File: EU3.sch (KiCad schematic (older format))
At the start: 52 parts, among them J301 ClockOut, J303 ClockIn, J304 Out0, J305 Out1, J306 Out2, J307 Out3, J308 Out4, J309 Out5, J310 Out6, J311 Out7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

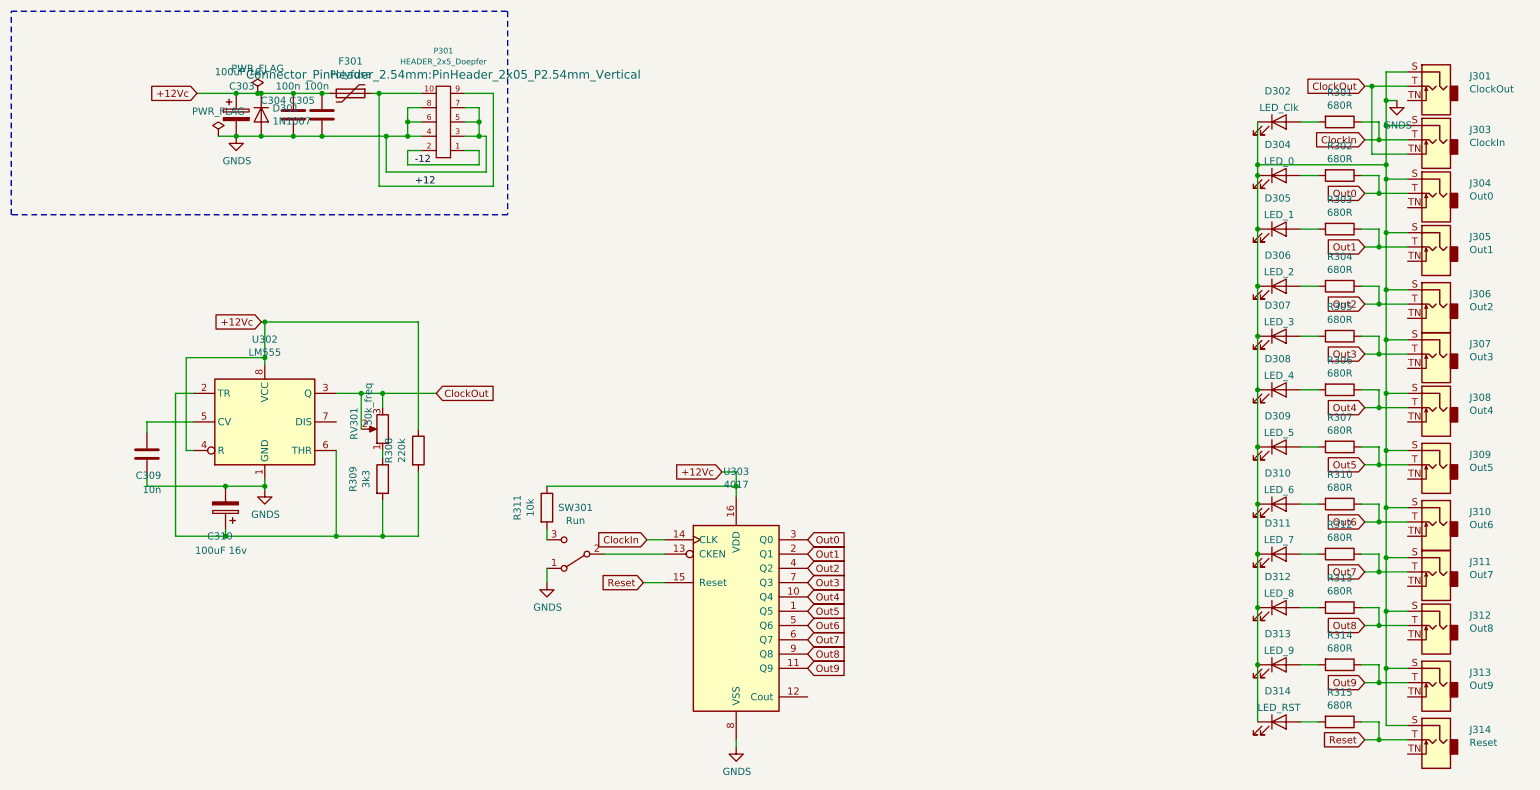
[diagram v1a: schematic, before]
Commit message: Counter with input protection and new stop/carry feature
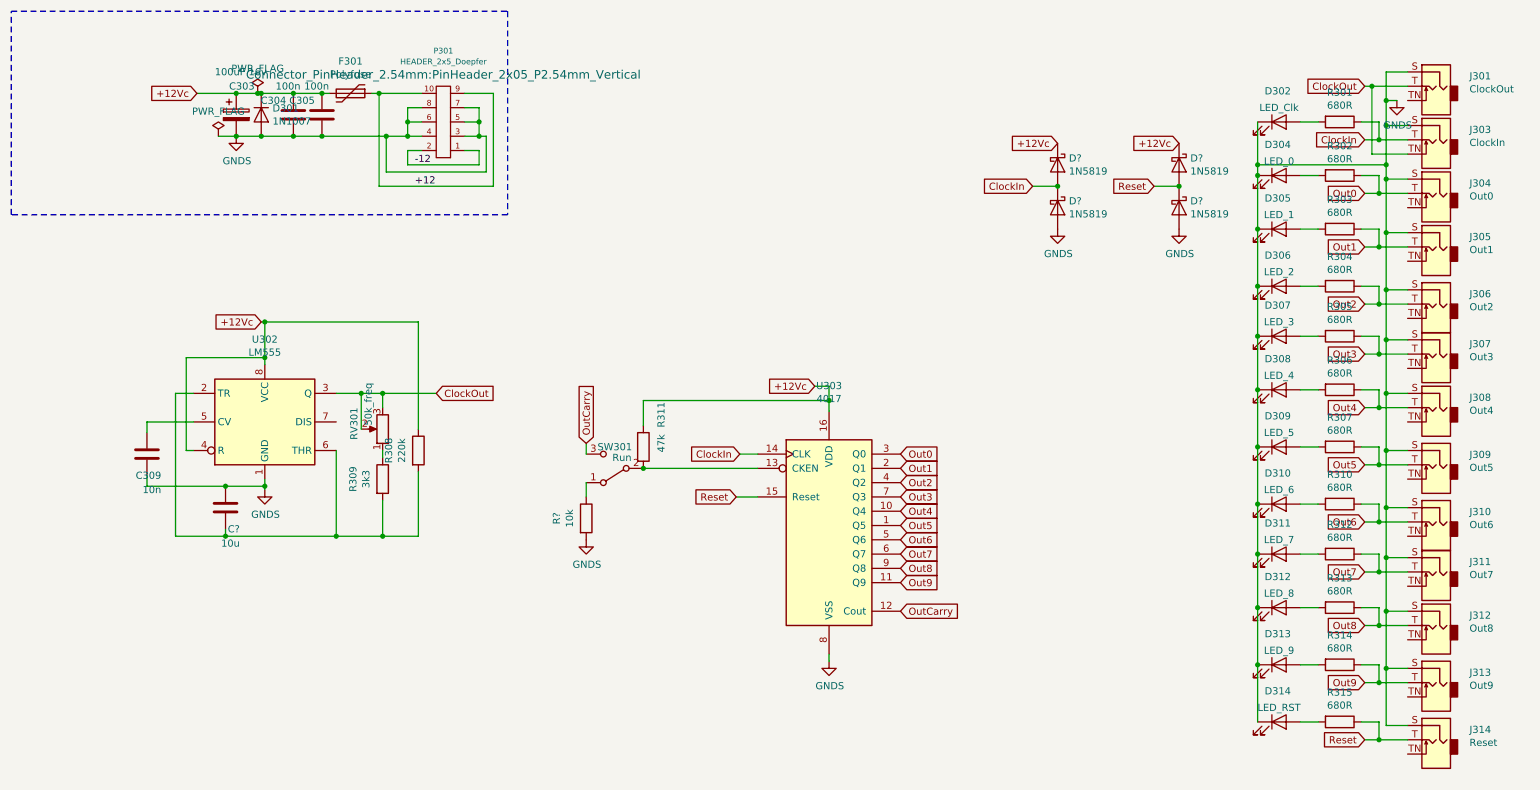
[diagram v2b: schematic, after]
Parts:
- removed C310: 100uF 16v, Capacitor_THT:CP_Radial_D5.0mm_P2.50mm, symbol Device:CP
- added C?: 10u, Capacitor_SMD:C_0805_2012Metric_Pad1.15x1.40mm_HandSolder, symbol Device:C
- added D? (x4): 1N5819, Diode_THT:D_DO-41_SOD81_P10.16mm_Horizontal, symbol Diode:1N5819
- added R?: 10k, Resistor_SMD:R_0805_2012Metric_Pad1.15x1.40mm_HandSolder, symbol Device:R
- R311: value 10k -> 47k
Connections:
- net +12Vc: now also D?.1 (K), D?.1 (K)
- net ClockIn: now also D?.1 (K), D?.2 (A)
- net GNDS: now also C?.2, D?.2 (A), D?.2 (A), R?.2; no longer SW301.1 (A)
- net Reset: now also D?.1 (K), D?.2 (A)
- net at R308.2, R309.2, U302.2 (TR)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: now also C?.1
- net OutCarry: now reaches U303.12 (Cout)
- net OutCarry: now also SW301.3 (C)
- net at SW301.2 (B), U303.13 (CKEN): now also R311.2
- new net: R?.1, SW301.1 (A)
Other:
- moved on the sheet: R311, SW301, U303
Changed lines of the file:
@@
 L 4xxx:4017 U303
 U 1 1 5C7AF44B
-P 5650 4725
-F 0 "U303" H 5650 5703 50  0000 C CNN
-F 1 "4017" H 5650 5612 50  0000 C CNN
-F 2 "Package_SO:SOIC-16_4.55x10.3mm_P1.27mm" H 5650 4725 50  0001 C CNN
-F 3 "http://www.intersil.com/content/dam/Intersil/documents/cd40/cd4017bms-22bms.pdf" H 5650 4725 50  0001 C CNN
-	1    5650 4725
+P 6300 4125
+F 0 "U303" H 6300 5103 50  0000 C CNN
+F 1 "4017" H 6300 5012 50  0000 C CNN
+F 2 "Package_SO:SOIC-16_4.55x10.3mm_P1.27mm" H 6300 4125 50  0001 C CNN
+F 3 "http://www.intersil.com/content/dam/Intersil/documents/cd40/cd4017bms-22bms.pdf" H 6300 4125 50  0001 C CNN
+	1    6300 4125
 	1    0    0    -1
 $EndComp
@@
 Wire Wire Line
 	1525 3775 1525 3850
-Wire Wire Line
-	1525 3850 2075 3850
 Connection ~ 2350 3850
 Wire Wire Line
 	2350 3850 2350 3800
-$Comp
-L Device:CP C?
-U 1 1 5C7BA0E3
-P 2075 4000
-AR Path="/5C7BA0E3" Ref="C?"  Part="1"
-AR Path="/5C781441/5C7BA0E3" Ref="C310"  Part="1"
-F 0 "C310" H 2025 4200 50  0000 L CNN
-F 1 "100uF 16v" H 1925 4300 50  0000 L CNN
-F 2 "Capacitor_THT:CP_Radial_D5.0mm_P2.50mm" H 2113 3850 50  0001 C CNN
-F 3 "~" H 2075 4000 50  0001 C CNN
-	1    2075 4000
-	-1   0    0    1
-$EndComp
-Connection ~ 2075 3850
-Wire Wire Line
-	2075 3850 2350 3850
 Wire Wire Line
 	2075 4200 2075 4150
@@
 Wire Wire Line
 	10050 1425 10150 1425
-Text GLabel 5025 4225 0    50   Input ~ 0
+Text GLabel 5675 3625 0    50   Input ~ 0
 ClockIn
 $Comp
@@
 Connection ~ 9300 3575
 Connection ~ 10200 3600
-Text GLabel 6150 5125 2    50   Input ~ 0
+Text GLabel 6800 4525 2    50   Input ~ 0
 Out9
-Text GLabel 6150 5025 2    50   Input ~ 0
+Text GLabel 6800 4425 2    50   Input ~ 0
 Out8
-Text GLabel 6150 4925 2    50   Input ~ 0
+Text GLabel 6800 4325 2    50   Input ~ 0
 Out7
-Text GLabel 6150 4825 2    50   Input ~ 0
+Text GLabel 6800 4225 2    50   Input ~ 0
 Out6
-Text GLabel 6150 4625 2    50   Input ~ 0
+Text GLabel 6800 4025 2    50   Input ~ 0
 Out4
-Text GLabel 6150 4525 2    50   Input ~ 0
+Text GLabel 6800 3925 2    50   Input ~ 0
 Out3
-Text GLabel 6150 4425 2    50   Input ~ 0
+Text GLabel 6800 3825 2    50   Input ~ 0
 Out2
-Text GLabel 6150 4325 2    50   Input ~ 0
+Text GLabel 6800 3725 2    50   Input ~ 0
 Out1
-Text GLabel 6150 4725 2    50   Input ~ 0
+Text GLabel 6800 4125 2    50   Input ~ 0
 Out5
-Text GLabel 6150 4225 2    50   Input ~ 0
+Text GLabel 6800 3625 2    50   Input ~ 0
 Out0
 $Comp
@@
 Connection ~ 9300 5100
 Connection ~ 10200 5125
-Text GLabel 5000 4525 0    50   Input ~ 0
+Text GLabel 5650 3925 0    50   Input ~ 0
 Reset
 Wire Wire Line
-	5025 4225 5150 4225
-Wire Wire Line
-	5000 4525 5150 4525
-Text GLabel 5550 3750 0    50   Input ~ 0
+	5675 3625 5800 3625
+Wire Wire Line
+	5650 3925 5800 3925
+Text GLabel 6200 3150 0    50   Input ~ 0
 +12Vc
 $Comp
 L power:GNDS #PWR?
 U 1 1 5C879D20
-P 5650 5675
+P 6300 5075
 AR Path="/5C879D20" Ref="#PWR?"  Part="1"
 AR Path="/5D60ED9A/5C879D20" Ref="#PWR?"  Part="1"
 AR Path="/5C781441/5C879D20" Ref="#PWR0124"  Part="1"
-F 0 "#PWR0124" H 5650 5425 50  0001 C CNN
-F 1 "GNDS" H 5655 5502 50  0000 C CNN
-F 2 "" H 5650 5675 50  0001 C CNN
-F 3 "" H 5650 5675 50  0001 C CNN
-	1    5650 5675
-	1    0    0    -1
-$EndComp
-Wire Wire Line
-	5650 5675 5650 5625
-Wire Wire Line
-	5650 3925 5650 3850
-Wire Wire Line
-	5650 3750 5550 3750
+F 0 "#PWR0124" H 6300 4825 50  0001 C CNN
+F 1 "GNDS" H 6305 4902 50  0000 C CNN
+F 2 "" H 6300 5075 50  0001 C CNN
+F 3 "" H 6300 5075 50  0001 C CNN
+	1    6300 5075
+	1    0    0    -1
+$EndComp
+Wire Wire Line
+	6300 5075 6300 5025
+Wire Wire Line
+	6300 3325 6300 3250
+Wire Wire Line
+	6300 3150 6200 3150
 $Comp
 L Switch:SW_SPDT SW?
 U 1 1 5C88D8DA
-P 4525 4325
+P 4800 3725
 AR Path="/5C88D8DA" Ref="SW?"  Part="1"
 AR Path="/5C781441/5C88D8DA" Ref="SW301"  Part="1"
-F 0 "SW301" H 4525 4000 50  0000 C CNN
-F 1 "Run" H 4525 4091 50  0000 C CNN
-F 2 "AJ-Dropbox-Kicad:SP1MS1" H 4525 4325 50  0001 C CNN
-F 3 "~" H 4525 4325 50  0001 C CNN
-	1    4525 4325
+F 0 "SW301" H 4800 3575 50  0000 C CNN
+F 1 "Run" H 4750 3650 50  0000 C CNN
+F 2 "AJ-Dropbox-Kicad:SP1MS1" H 4800 3725 50  0001 C CNN
+F 3 "~" H 4800 3725 50  0001 C CNN
+	1    4800 3725
 	-1   0    0    1
 $EndComp
-Wire Wire Line
-	5150 4325 4725 4325
 $Comp
 L Device:R R?
 U 1 1 5C8AA357
-P 4325 4000
+P 5000 3575
 AR Path="/5C8AA357" Ref="R?"  Part="1"
 AR Path="/5C781441/5C8AA357" Ref="R311"  Part="1"
-F 0 "R311" V 4118 4000 50  0000 C CNN
-F 1 "10k" V 4209 4000 50  0000 C CNN
-F 2 "Resistor_SMD:R_0805_2012Metric_Pad1.15x1.40mm_HandSolder" V 4255 4000 50  0001 C CNN
-F 3 "~" H 4325 4000 50  0001 C CNN
-	1    4325 4000
+F 0 "R311" V 5125 3800 50  0000 C CNN
+F 1 "47k" V 5125 3600 50  0000 C CNN
+F 2 "Resistor_SMD:R_0805_2012Metric_Pad1.15x1.40mm_HandSolder" V 4930 3575 50  0001 C CNN
+F 3 "~" H 5000 3575 50  0001 C CNN
+	1    5000 3575
 	1    0    0    -1
 $EndComp
@@
 L power:GNDS #PWR?
 U 1 1 5C8AA43A
-P 4325 4525
+P 4600 4225
 AR Path="/5C8AA43A" Ref="#PWR?"  Part="1"
 AR Path="/5D60ED9A/5C8AA43A" Ref="#PWR?"  Part="1"
 AR Path="/5C781441/5C8AA43A" Ref="#PWR0125"  Part="1"
-F 0 "#PWR0125" H 4325 4275 50  0001 C CNN
-F 1 "GNDS" H 4330 4352 50  0000 C CNN
-F 2 "" H 4325 4525 50  0001 C CNN
-F 3 "" H 4325 4525 50  0001 C CNN
-	1    4325 4525
-	1    0    0    -1
-$EndComp
-Wire Wire Line
-	4325 3850 5650 3850
-Connection ~ 5650 3850
-Wire Wire Line
-	5650 3850 5650 3750
-Wire Wire Line
-	4325 4150 4325 4225
-Wire Wire Line
-	4325 4525 4325 4425
+F 0 "#PWR0125" H 4600 3975 50  0001 C CNN
+F 1 "GNDS" H 4605 4052 50  0000 C CNN
+F 2 "" H 4600 4225 50  0001 C CNN
+F 3 "" H 4600 4225 50  0001 C CNN
+	1    4600 4225
+	1    0    0    -1
+$EndComp
+Connection ~ 6300 3250
+Wire Wire Line
+	6300 3250 6300 3150
+Wire Wire Line
+	4600 3550 4600 3625
+Wire Wire Line
+	4600 3925 4600 3825
 Wire Wire Line
 	1875 1100 2150 1100
@@
 Text Label 3400 1750 0    50   ~ 0
 +12
+Text GLabel 7725 1750 0    50   Input ~ 0
+ClockIn
+Text GLabel 8575 1750 0    50   Input ~ 0
+Reset
+$Comp
+L Diode:1N5819 D?
+U 1 1 5CCD6095
+P 7900 1600
+F 0 "D?" V 7854 1679 50  0000 L CNN
+F 1 "1N5819" V 7945 1679 50  0000 L CNN
+F 2 "Diode_THT:D_DO-41_SOD81_P10.16mm_Horizontal" H 7900 1425 50  0001 C CNN
+F 3 "http://www.vishay.com/docs/88525/1n5817.pdf" H 7900 1600 50  0001 C CNN
+	1    7900 1600
+	0    1    1    0
+$EndComp
+$Comp
+L Diode:1N5819 D?
+U 1 1 5CCD6FDF
+P 7900 1900
+F 0 "D?" V 7854 1979 50  0000 L CNN
+F 1 "1N5819" V 7945 1979 50  0000 L CNN
+F 2 "Diode_THT:D_DO-41_SOD81_P10.16mm_Horizontal" H 7900 1725 50  0001 C CNN
+F 3 "http://www.vishay.com/docs/88525/1n5817.pdf" H 7900 1900 50  0001 C CNN
+	1    7900 1900
+	0    1    1    0
+$EndComp
+$Comp
+L power:GNDS #PWR?
+U 1 1 5CCD768A
+P 7900 2050
+AR Path="/5CCD768A" Ref="#PWR?"  Part="1"
+AR Path="/5D60ED9A/5CCD768A" Ref="#PWR?"  Part="1"
+AR Path="/5C781441/5CCD768A" Ref="#PWR?"  Part="1"
+F 0 "#PWR?" H 7900 1800 50  0001 C CNN
+F 1 "GNDS" H 7905 1877 50  0000 C CNN
+F 2 "" H 7900 2050 50  0001 C CNN
+F 3 "" H 7900 2050 50  0001 C CNN
+	1    7900 2050
+	1    0    0    -1
+$EndComp
+Text GLabel 7900 1450 0    50   Input ~ 0
++12Vc
+Wire Wire Line
+	7725 1750 7900 1750
+Connection ~ 7900 1750
+$Comp
+L Diode:1N5819 D?
+U 1 1 5CCE2123
+P 8750 1600
+F 0 "D?" V 8704 1679 50  0000 L CNN
+F 1 "1N5819" V 8795 1679 50  0000 L CNN
+F 2 "Diode_THT:D_DO-41_SOD81_P10.16mm_Horizontal" H 8750 1425 50  0001 C CNN
+F 3 "http://www.vishay.com/docs/88525/1n5817.pdf" H 8750 1600 50  0001 C CNN
+	1    8750 1600
+	0    1    1    0
+$EndComp
+$Comp
+L Diode:1N5819 D?
+U 1 1 5CCE212D
+P 8750 1900
+F 0 "D?" V 8704 1979 50  0000 L CNN
+F 1 "1N5819" V 8795 1979 50  0000 L CNN
+F 2 "Diode_THT:D_DO-41_SOD81_P10.16mm_Horizontal" H 8750 1725 50  0001 C CNN
+F 3 "http://www.vishay.com/docs/88525/1n5817.pdf" H 8750 1900 50  0001 C CNN
+	1    8750 1900
+	0    1    1    0
+$EndComp
+$Comp
+L power:GNDS #PWR?
+U 1 1 5CCE2137
+P 8750 2050
+AR Path="/5CCE2137" Ref="#PWR?"  Part="1"
+AR Path="/5D60ED9A/5CCE2137" Ref="#PWR?"  Part="1"
+AR Path="/5C781441/5CCE2137" Ref="#PWR?"  Part="1"
+F 0 "#PWR?" H 8750 1800 50  0001 C CNN
+F 1 "GNDS" H 8755 1877 50  0000 C CNN
+F 2 "" H 8750 2050 50  0001 C CNN
+F 3 "" H 8750 2050 50  0001 C CNN
+	1    8750 2050
+	1    0    0    -1
+$EndComp
+Text GLabel 8750 1450 0    50   Input ~ 0
++12Vc
+Wire Wire Line
+	8575 1750 8750 1750
+Connection ~ 8750 1750
+Wire Wire Line
+	5000 3725 5800 3725
+Wire Wire Line
+	5000 3425 5000 3250
+Wire Wire Line
+	5000 3250 6300 3250
+Connection ~ 5000 3725
+Text GLabel 6800 4725 2    50   Input ~ 0
+OutCarry
+Text GLabel 4600 3550 1    50   Input ~ 0
+OutCarry
+$Comp
+L Device:R R?
+U 1 1 5CD1A27B
+P 4600 4075
+AR Path="/5CD1A27B" Ref="R?"  Part="1"
+AR Path="/5C781441/5CD1A27B" Ref="R?"  Part="1"
+F 0 "R?" V 4393 4075 50  0000 C CNN
+F 1 "10k" V 4484 4075 50  0000 C CNN
+F 2 "Resistor_SMD:R_0805_2012Metric_Pad1.15x1.40mm_HandSolder" V 4530 4075 50  0001 C CNN
+F 3 "~" H 4600 4075 50  0001 C CNN
+	1    4600 4075
+	1    0    0    -1
+$EndComp
+Wire Wire Line
+	1525 3850 2075 3850
+$Comp
+L Device:C C?
+U 1 1 5CD1AA3C
+P 2075 4000
+AR Path="/5CD1AA3C" Ref="C?"  Part="1"
+AR Path="/5C781441/5CD1AA3C" Ref="C?"  Part="1"
+F 0 "C?" H 1975 4150 50  0000 L CNN
+F 1 "10u" H 1975 4250 50  0000 L CNN
+F 2 "Capacitor_SMD:C_0805_2012Metric_Pad1.15x1.40mm_HandSolder" H 2113 3850 50  0001 C CNN
+F 3 "~" H 2075 4000 50  0001 C CNN
+	1    2075 4000
+	-1   0    0    1
+$EndComp
+Connection ~ 2075 3850
+Wire Wire Line
+	2075 3850 2350 3850
 $EndSCHEMATC

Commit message: Rev 1,2 Counter Resistor on LED
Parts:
- R301, R302, R303, R304, R305, R306, R307, R310, R312, R313, R314, R315: value 680R -> 4k7
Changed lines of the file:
@@
 AR Path="/5C781441/5C7E5BC0" Ref="R301"  Part="1"
 F 0 "R301" V 9668 1300 50  0000 C CNN
-F 1 "680R" V 9759 1300 50  0000 C CNN
+F 1 "4k7" V 9759 1300 50  0000 C CNN
 F 2 "Resistor_SMD:R_0805_2012Metric_Pad1.15x1.40mm_HandSolder" V 9805 1300 50  0001 C CNN
 F 3 "~" H 9875 1300 50  0001 C CNN
@@
 AR Path="/5C781441/5C827C46" Ref="R302"  Part="1"
 F 0 "R302" V 9668 1675 50  0000 C CNN
-F 1 "680R" V 9759 1675 50  0000 C CNN
+F 1 "4k7" V 9759 1675 50  0000 C CNN
 F 2 "Resistor_SMD:R_0805_2012Metric_Pad1.15x1.40mm_HandSolder" V 9805 1675 50  0001 C CNN
 F 3 "~" H 9875 1675 50  0001 C CNN
@@
 AR Path="/5C781441/5C831A34" Ref="R303"  Part="1"
 F 0 "R303" V 9668 2050 50  0000 C CNN
-F 1 "680R" V 9759 2050 50  0000 C CNN
+F 1 "4k7" V 9759 2050 50  0000 C CNN
 F 2 "Resistor_SMD:R_0805_2012Metric_Pad1.15x1.40mm_HandSolder" V 9805 2050 50  0001 C CNN
 F 3 "~" H 9875 2050 50  0001 C CNN
@@
 AR Path="/5C781441/5C8355AA" Ref="R304"  Part="1"
 F 0 "R304" V 9668 2450 50  0000 C CNN
-F 1 "680R" V 9759 2450 50  0000 C CNN
+F 1 "4k7" V 9759 2450 50  0000 C CNN
 F 2 "Resistor_SMD:R_0805_2012Metric_Pad1.15x1.40mm_HandSolder" V 9805 2450 50  0001 C CNN
 F 3 "~" H 9875 2450 50  0001 C CNN
@@
 AR Path="/5C781441/5C83D871" Ref="R305"  Part="1"
 F 0 "R305" V 9668 2800 50  0000 C CNN
-F 1 "680R" V 9759 2800 50  0000 C CNN
+F 1 "4k7" V 9759 2800 50  0000 C CNN
 F 2 "Resistor_SMD:R_0805_2012Metric_Pad1.15x1.40mm_HandSolder" V 9805 2800 50  0001 C CNN
 F 3 "~" H 9875 2800 50  0001 C CNN
@@
 AR Path="/5C781441/5C83D884" Ref="R306"  Part="1"
 F 0 "R306" V 9668 3175 50  0000 C CNN
-F 1 "680R" V 9759 3175 50  0000 C CNN
+F 1 "4k7" V 9759 3175 50  0000 C CNN
 F 2 "Resistor_SMD:R_0805_2012Metric_Pad1.15x1.40mm_HandSolder" V 9805 3175 50  0001 C CNN
 F 3 "~" H 9875 3175 50  0001 C CNN
@@
 AR Path="/5C781441/5C83D897" Ref="R307"  Part="1"
 F 0 "R307" V 9668 3575 50  0000 C CNN
-F 1 "680R" V 9759 3575 50  0000 C CNN
+F 1 "4k7" V 9759 3575 50  0000 C CNN
 F 2 "Resistor_SMD:R_0805_2012Metric_Pad1.15x1.40mm_HandSolder" V 9805 3575 50  0001 C CNN
 F 3 "~" H 9875 3575 50  0001 C CNN
@@
 AR Path="/5C781441/5C843B49" Ref="R310"  Part="1"
 F 0 "R310" V 9668 3975 50  0000 C CNN
-F 1 "680R" V 9759 3975 50  0000 C CNN
+F 1 "4k7" V 9759 3975 50  0000 C CNN
 F 2 "Resistor_SMD:R_0805_2012Metric_Pad1.15x1.40mm_HandSolder" V 9805 3975 50  0001 C CNN
 F 3 "~" H 9875 3975 50  0001 C CNN
@@
 AR Path="/5C781441/5C843B75" Ref="R312"  Part="1"
 F 0 "R312" V 9668 4325 50  0000 C CNN
-F 1 "680R" V 9759 4325 50  0000 C CNN
+F 1 "4k7" V 9759 4325 50  0000 C CNN
 F 2 "Resistor_SMD:R_0805_2012Metric_Pad1.15x1.40mm_HandSolder" V 9805 4325 50  0001 C CNN
 F 3 "~" H 9875 4325 50  0001 C CNN
@@
 AR Path="/5C781441/5C843B88" Ref="R313"  Part="1"
 F 0 "R313" V 9668 4700 50  0000 C CNN
-F 1 "680R" V 9759 4700 50  0000 C CNN
+F 1 "4k7" V 9759 4700 50  0000 C CNN
 F 2 "Resistor_SMD:R_0805_2012Metric_Pad1.15x1.40mm_HandSolder" V 9805 4700 50  0001 C CNN
 F 3 "~" H 9875 4700 50  0001 C CNN
@@
 AR Path="/5C781441/5C843B9B" Ref="R314"  Part="1"
 F 0 "R314" V 9668 5100 50  0000 C CNN
-F 1 "680R" V 9759 5100 50  0000 C CNN
+F 1 "4k7" V 9759 5100 50  0000 C CNN
 F 2 "Resistor_SMD:R_0805_2012Metric_Pad1.15x1.40mm_HandSolder" V 9805 5100 50  0001 C CNN
 F 3 "~" H 9875 5100 50  0001 C CNN
@@
 AR Path="/5C781441/5C8555D7" Ref="R315"  Part="1"
 F 0 "R315" V 9668 5500 50  0000 C CNN
-F 1 "680R" V 9759 5500 50  0000 C CNN
+F 1 "4k7" V 9759 5500 50  0000 C CNN
 F 2 "Resistor_SMD:R_0805_2012Metric_Pad1.15x1.40mm_HandSolder" V 9805 5500 50  0001 C CNN
 F 3 "~" H 9875 5500 50  0001 C CNN
